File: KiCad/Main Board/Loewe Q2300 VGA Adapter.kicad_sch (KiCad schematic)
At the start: 63 parts, among them Q1 BC847B, Q10 BC847B, Q14 BC847B, Q2 BC847B, Q3 BC847B, Q4 BC847B, Q5 BC847B, Q6 BC847B, U1 74HCT86

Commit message: Change L1 inductor footprint to 1210 (TDK/EPCOS NLCV32T-4R7M-EF).
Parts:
- L1: footprint Inductor_SMD:L_1206_3216Metric -> Inductor_SMD:L_1210_3225Metric_Pad1.42x2.65mm_HandSolder
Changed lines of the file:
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@@
 			)
 		)
-		(property "Footprint" "Inductor_SMD:L_1206_3216Metric"
+		(property "Footprint" "Inductor_SMD:L_1210_3225Metric_Pad1.42x2.65mm_HandSolder"
 			(at 199.39 99.06 0)
 			(effects

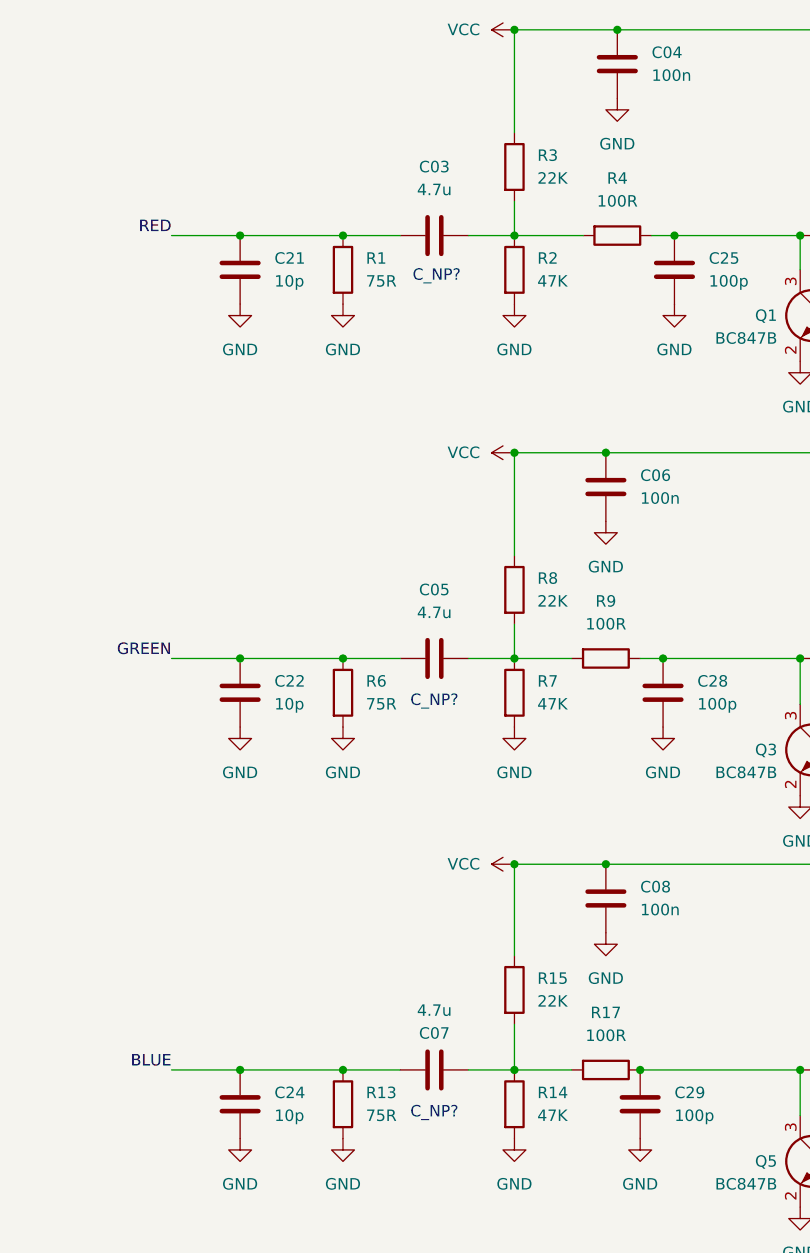
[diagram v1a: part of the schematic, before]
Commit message: Change RGB input capacitors footprints to Capacitor_SMD:CP_Elec_4x5.4. Reverse RGB capacitors polarity.
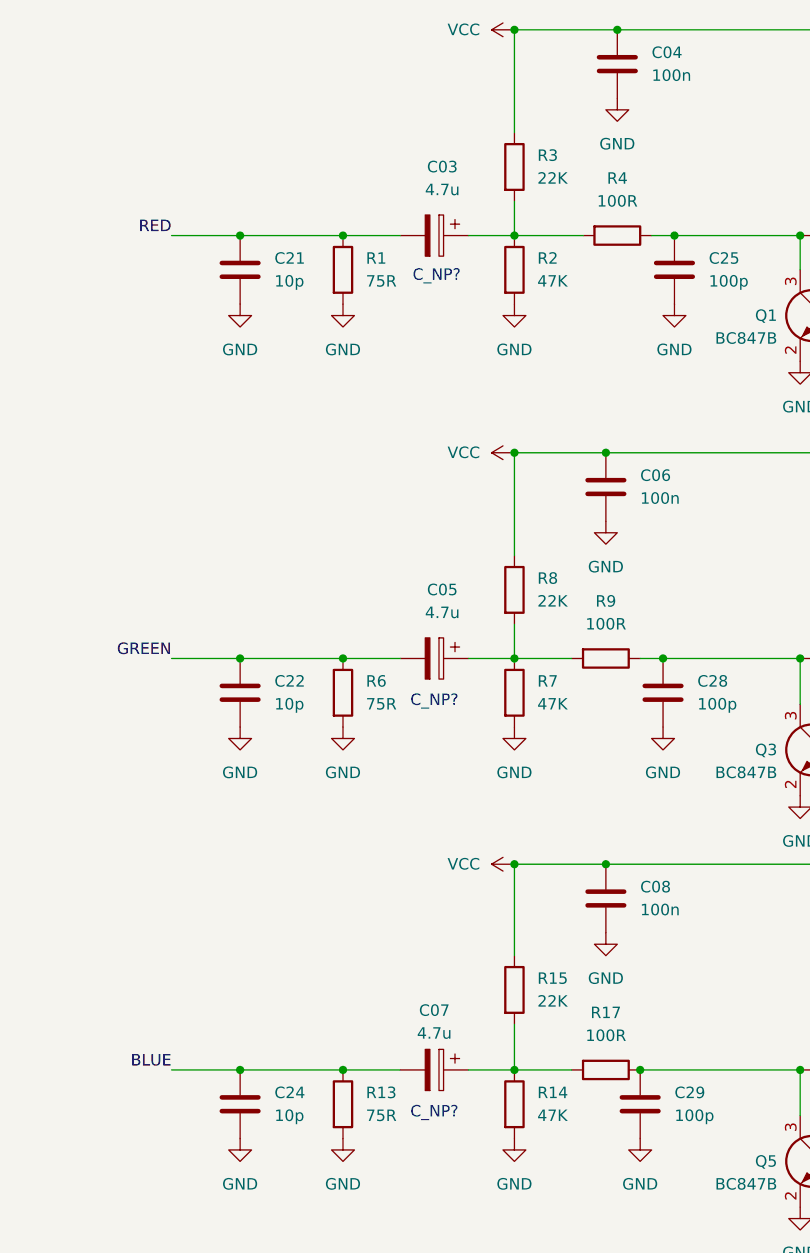
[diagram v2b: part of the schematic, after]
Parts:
- C03, C05, C07: footprint Capacitor_SMD:CP_Elec_6.3x5.4 -> Capacitor_SMD:CP_Elec_4x5.4; symbol Device:C -> Device:C_Polarized
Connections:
- net BLUE: now also C07.2; no longer C07.1
- net GREEN: now also C05.2; no longer C05.1
- net RED: now also C03.2; no longer C03.1
- net at R14.1, R15.2, R17.2: now also C07.1; no longer C07.2
- net at R7.1, R8.2, R9.2: now also C05.1; no longer C05.2
- net at R2.1, R3.2, R4.2: now also C03.1; no longer C03.2
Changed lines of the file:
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@@
 	)
 	(junction
-		(at 162.56 93.98)
+		(at 92.71 36.83)
 		(diameter 0)
 		(color 0 0 0 0)
 	)
 	(junction
-		(at 121.92 60.96)
+		(at 162.56 93.98)
 		(diameter 0)
 		(color 0 0 0 0)
 	)
 	(junction
-		(at 92.71 83.82)
+		(at 121.92 60.96)
 		(diameter 0)
 		(color 0 0 0 0)
@@
 	)
 	(junction
+		(at 92.71 129.54)
+		(diameter 0)
+		(color 0 0 0 0)
+	)
+	(junction
 		(at 111.76 60.96)
 		(diameter 0)
@@
 	)
 	(junction
-		(at 129.54 36.83)
+		(at 92.71 83.82)
 		(diameter 0)
 		(color 0 0 0 0)
 	)
 	(junction
-		(at 162.56 139.7)
+		(at 129.54 36.83)
 		(diameter 0)
 		(color 0 0 0 0)
 	)
 	(junction
-		(at 111.76 83.82)
+		(at 162.56 139.7)
 		(diameter 0)
 		(color 0 0 0 0)
 	)
 	(junction
-		(at 113.03 195.58)
+		(at 111.76 83.82)
 		(diameter 0)
 		(color 0 0 0 0)
 	)
 	(junction
-		(at 92.71 129.54)
+		(at 113.03 195.58)
 		(diameter 0)
 		(color 0 0 0 0)
@@
 	)
 	(junction
-		(at 92.71 36.83)
-		(diameter 0)
-		(color 0 0 0 0)
-	)
-	(junction
 		(at 101.6 195.58)
 		(diameter 0)
@@
 	(wire
 		(pts
-			(xy 99.06 129.54) (xy 92.71 129.54)
-		)
-		(stroke
-			(width 0)
-			(type default)
-		)
-	)
-	(wire
-		(pts
 			(xy 210.82 104.14) (xy 217.17 104.14)
 		)
@@
 	(wire
 		(pts
+			(xy 92.71 129.54) (xy 99.06 129.54)
+		)
+		(stroke
+			(width 0)
+			(type default)
+		)
+	)
+	(wire
+		(pts
 			(xy 111.76 60.96) (xy 121.92 60.96)
 		)
@@
 	(wire
 		(pts
-			(xy 106.68 83.82) (xy 111.76 83.82)
+			(xy 92.71 36.83) (xy 99.06 36.83)
 		)
 		(stroke
@@
 	(wire
 		(pts
-			(xy 129.54 36.83) (xy 127 36.83)
+			(xy 106.68 36.83) (xy 111.76 36.83)
 		)
 		(stroke
@@
 	(wire
 		(pts
-			(xy 129.54 36.83) (xy 143.51 36.83)
+			(xy 129.54 36.83) (xy 127 36.83)
 		)
 		(stroke
@@
 	(wire
 		(pts
-			(xy 81.28 190.5) (xy 91.44 190.5)
+			(xy 129.54 36.83) (xy 143.51 36.83)
 		)
 		(stroke
@@
 	(wire
 		(pts
-			(xy 73.66 83.82) (xy 81.28 83.82)
+			(xy 81.28 190.5) (xy 91.44 190.5)
 		)
 		(stroke
@@
 	(wire
 		(pts
-			(xy 217.17 99.06) (xy 205.74 99.06)
+			(xy 73.66 83.82) (xy 81.28 83.82)
 		)
 		(stroke
@@
 	(wire
 		(pts
-			(xy 111.76 124.46) (xy 111.76 129.54)
+			(xy 217.17 99.06) (xy 205.74 99.06)
 		)
 		(stroke
@@
 	(wire
 		(pts
-			(xy 214.63 91.44) (xy 217.17 91.44)
+			(xy 111.76 124.46) (xy 111.76 129.54)
 		)
 		(stroke
@@
 	(wire
 		(pts
-			(xy 162.56 139.7) (xy 158.75 139.7)
+			(xy 214.63 91.44) (xy 217.17 91.44)
 		)
 		(stroke
@@
 	(wire
 		(pts
-			(xy 106.68 36.83) (xy 111.76 36.83)
+			(xy 162.56 139.7) (xy 158.75 139.7)
 		)
 		(stroke
@@
 	(wire
 		(pts
-			(xy 64.77 190.5) (xy 73.66 190.5)
+			(xy 92.71 83.82) (xy 99.06 83.82)
 		)
 		(stroke
@@
 	(wire
 		(pts
-			(xy 185.42 81.28) (xy 185.42 88.9)
+			(xy 64.77 190.5) (xy 73.66 190.5)
 		)
 		(stroke
@@
 	(wire
 		(pts
-			(xy 203.2 99.06) (xy 203.2 96.52)
+			(xy 185.42 81.28) (xy 185.42 88.9)
 		)
 		(stroke
@@
 	(wire
 		(pts
-			(xy 92.71 36.83) (xy 99.06 36.83)
+			(xy 203.2 99.06) (xy 203.2 96.52)
 		)
 		(stroke
@@
 	(wire
 		(pts
-			(xy 92.71 83.82) (xy 99.06 83.82)
+			(xy 106.68 129.54) (xy 111.76 129.54)
 		)
 		(stroke
@@
 	(wire
 		(pts
-			(xy 121.92 60.96) (xy 151.13 60.96)
+			(xy 106.68 83.82) (xy 111.76 83.82)
 		)
 		(stroke
@@
 	(wire
 		(pts
-			(xy 215.9 81.28) (xy 217.17 81.28)
+			(xy 121.92 60.96) (xy 151.13 60.96)
 		)
 		(stroke
@@
 	(wire
 		(pts
-			(xy 106.68 129.54) (xy 111.76 129.54)
+			(xy 215.9 81.28) (xy 217.17 81.28)
 		)
 		(stroke
@@
 	)
 	(symbol
-		(lib_id "Device:C")
-		(at 102.87 129.54 90)
+		(lib_name "C_Polarized_3")
+		(lib_id "Device:C_Polarized")
+		(at 102.87 129.54 270)
 		(unit 1)
 		(exclude_from_sim no)
@@
 		(dnp no)
 		(property "Reference" "C07"
-			(at 102.87 125.476 90)
+			(at 102.87 122.936 90)
 			(effects
 				(font
@@
 		)
 		(property "Value" "4.7u"
-			(at 102.87 122.936 90)
+			(at 102.87 125.476 90)
 			(effects
 				(font
@@
 			)
 		)
-		(property "Footprint" "Capacitor_SMD:CP_Elec_6.3x5.4"
-			(at 106.68 128.5748 0)
+		(property "Footprint" "Capacitor_SMD:CP_Elec_4x5.4"
+			(at 99.06 130.5052 0)
 			(effects
 				(font
@@
 			)
 		)
-		(property "Description" "Unpolarized capacitor"
+		(property "Description" "Polarized capacitor"
 			(at 102.87 129.54 0)
 			(effects
@@
 	)
 	(symbol
-		(lib_id "Device:C")
-		(at 102.87 83.82 90)
+		(lib_name "C_Polarized_1")
+		(lib_id "Device:C_Polarized")
+		(at 102.87 83.82 270)
 		(unit 1)
 		(exclude_from_sim no)
@@
 		(fields_autoplaced yes)
 		(property "Reference" "C05"
-			(at 102.87 76.2 90)
+			(at 103.759 76.2 90)
 			(effects
 				(font
@@
 		)
 		(property "Value" "4.7u"
-			(at 102.87 78.74 90)
+			(at 103.759 78.74 90)
 			(effects
 				(font
@@
 			)
 		)
-		(property "Footprint" "Capacitor_SMD:CP_Elec_6.3x5.4"
-			(at 106.68 82.8548 0)
+		(property "Footprint" "Capacitor_SMD:CP_Elec_4x5.4"
+			(at 99.06 84.7852 0)
 			(effects
 				(font
@@
 			)
 		)
-		(property "Description" "Unpolarized capacitor"
+		(property "Description" "Polarized capacitor"
 			(at 102.87 83.82 0)
 			(effects
@@
 	)
 	(symbol
-		(lib_id "Device:C")
-		(at 102.87 36.83 90)
+		(lib_name "C_Polarized_2")
+		(lib_id "Device:C_Polarized")
+		(at 102.87 36.83 270)
 		(unit 1)
 		(exclude_from_sim no)
@@
 		(fields_autoplaced yes)
 		(property "Reference" "C03"
-			(at 102.87 29.21 90)
+			(at 103.759 29.21 90)
 			(effects
 				(font
@@
 		)
 		(property "Value" "4.7u"
-			(at 102.87 31.75 90)
+			(at 103.759 31.75 90)
 			(effects
 				(font
@@
 			)
 		)
-		(property "Footprint" "Capacitor_SMD:CP_Elec_6.3x5.4"
-			(at 106.68 35.8648 0)
+		(property "Footprint" "Capacitor_SMD:CP_Elec_4x5.4"
+			(at 99.06 37.7952 0)
 			(effects
 				(font
@@
 			)
 		)
-		(property "Description" "Unpolarized capacitor"
+		(property "Description" "Polarized capacitor"
 			(at 102.87 36.83 0)
 			(effects

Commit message: Replace JST XH 2.50 mm with custom 2.54 mm.
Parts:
- W02, W03: footprint Connector_JST:JST_XH_B10B-XH-A_1x10_P2.50mm_Vertical -> JST_XH_S10B_2.54mm:JST_XH_B10B-XH-A_1x10_P2.54mm_Vertical
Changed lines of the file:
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@@
 			)
 		)
-		(property "Footprint" "Connector_JST:JST_XH_B10B-XH-A_1x10_P2.50mm_Vertical"
+		(property "Footprint" "JST_XH_S10B_2.54mm:JST_XH_B10B-XH-A_1x10_P2.54mm_Vertical"
 			(at 222.25 91.44 0)
 			(effects
@@
 			)
 		)
-		(property "Footprint" "Connector_JST:JST_XH_B10B-XH-A_1x10_P2.50mm_Vertical"
+		(property "Footprint" "JST_XH_S10B_2.54mm:JST_XH_B10B-XH-A_1x10_P2.54mm_Vertical"
 			(at 29.21 83.82 0)
 			(effects

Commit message: Replace footprint for RGB input capacitors with custom combined SMD/THT one.
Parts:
- C03, C05, C07: footprint Capacitor_SMD:CP_Elec_4x5.4 -> Capacitor_SMD_THT:CP_Elec_4x5.4
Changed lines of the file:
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@@
 			)
 		)
-		(property "Footprint" "Capacitor_SMD:CP_Elec_4x5.4"
+		(property "Footprint" "Capacitor_SMD_THT:CP_Elec_4x5.4"
 			(at 99.06 130.5052 0)
 			(effects
@@
 			)
 		)
-		(property "Footprint" "Capacitor_SMD:CP_Elec_4x5.4"
+		(property "Footprint" "Capacitor_SMD_THT:CP_Elec_4x5.4"
 			(at 99.06 84.7852 0)
 			(effects
@@
 			)
 		)
-		(property "Footprint" "Capacitor_SMD:CP_Elec_4x5.4"
+		(property "Footprint" "Capacitor_SMD_THT:CP_Elec_4x5.4"
 			(at 99.06 37.7952 0)
 			(effects
